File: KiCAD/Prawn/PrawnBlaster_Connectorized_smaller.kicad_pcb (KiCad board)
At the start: 2 copper layers, 93 x 58.4 mm, 37 parts, among them IC1 74LVT245D,118, J1 PWR SEL, J2 Ext. Clock, J3 Ext. Trig., J4 Pseudoclock 3, J5 Pseudoclock 1, J6 Pseudoclock 2, J7 Pseudoclock 0, J8 EXT PWR, U2 74LVC1G34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

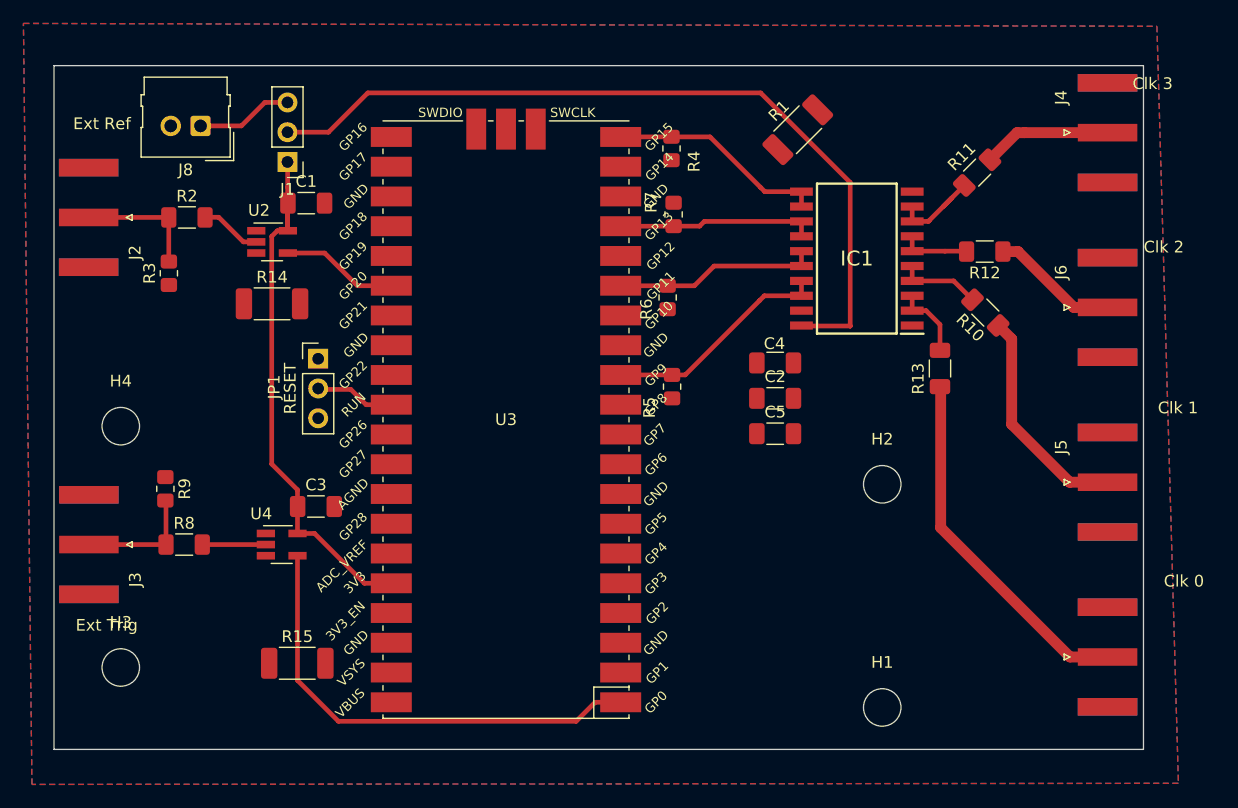
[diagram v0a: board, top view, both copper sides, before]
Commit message: Fixed trace and added gerber file
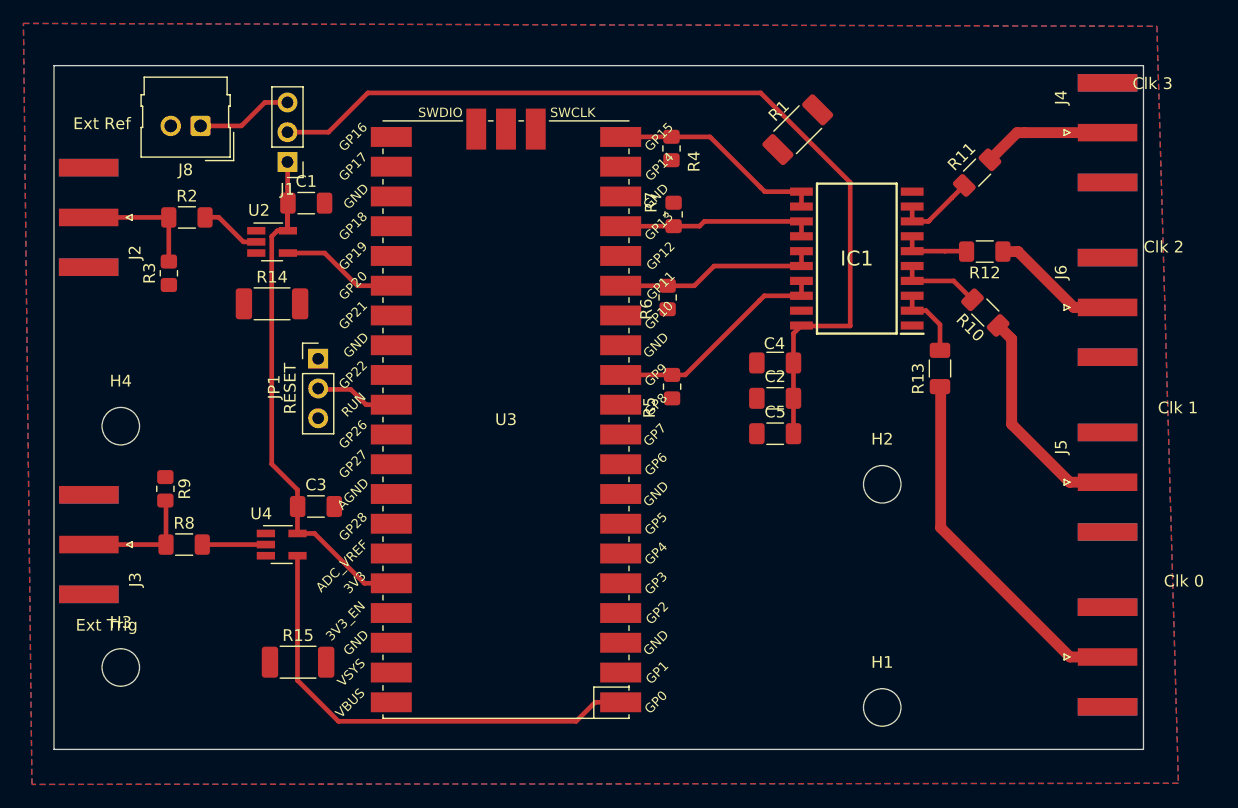
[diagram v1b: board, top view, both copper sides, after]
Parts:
- moved R15 0.11 mm to (107.9, 108.1)
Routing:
- net Power Supply: track 69.0 -> 78.5 mm
- net Net-(IC1-A6): track 8.03 -> 7.00 mm
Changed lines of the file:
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@@
   )
   (footprint "Resistor_SMD:R_2010_5025Metric_Pad1.40x2.65mm_HandSolder" (layer "F.Cu")
-    (at 107.8082 108.1804)
+    (at 107.876 108.0892)
     (descr "Resistor SMD 2010 (5025 Metric), square (rectangular) end terminal, IPC_7351 nominal with elongated pad for handsoldering. (Body size source: IPC-SM-782 page 72, https://www.pcb-3d.com/wordpress/wp-content/uploads/ipc-sm-782a_amendment_1_and_2.pdf), generated with kicad-footprint-generator")
     (tags "resistor handsolder")
@@
   (segment (start 134.5192 63.2462) (end 139.742 63.2462) (width 0.4) (layer "F.Cu") (net 6))
   (segment (start 139.752 63.2362) (end 139.762 63.2462) (width 0.4) (layer "F.Cu") (net 6))
-  (segment (start 162.947 69.1912) (end 163.677 68.4612) (width 0.4) (layer "F.Cu") (net 7))
   (segment (start 160.297 70.4612) (end 161.687 70.4612) (width 0.4) (layer "F.Cu") (net 7))
   (segment (start 161.742 70.3962) (end 163.677 68.4612) (width 0.4) (layer "F.Cu") (net 7))
@@
   (segment (start 113.6866 86.1108) (end 112.3796 84.8038) (width 0.4) (layer "F.Cu") (net 49))
   (segment (start 112.3796 84.8038) (end 109.6716 84.8038) (width 0.4) (layer "F.Cu") (net 49))
+  (segment (start 150.1642 80.034) (end 150.1642 88.5834) (width 0.4) (layer "F.Cu") (net 51))
   (segment (start 113.8262 59.4924) (end 147.3622 59.4924) (width 0.4) (layer "F.Cu") (net 51))
   (segment (start 110.4732 62.8454) (end 113.8262 59.4924) (width 0.4) (layer "F.Cu") (net 51))
@@
   (segment (start 106.9702 62.8454) (end 110.4732 62.8454) (width 0.4) (layer "F.Cu") (net 51))
   (segment (start 147.3622 59.4924) (end 155.0072 67.1374) (width 0.4) (layer "F.Cu") (net 51))
-  (segment (start 155.0046 79.3888) (end 155.012 79.3962) (width 0.4) (layer "F.Cu") (net 51))
-  (segment (start 155.0072 79.3862) (end 155.0046 79.3888) (width 0.4) (layer "F.Cu") (net 51))
   (segment (start 150.847 79.3512) (end 150.8846 79.3888) (width 0.4) (layer "F.Cu") (net 51))
+  (segment (start 150.847 79.3512) (end 150.1642 80.034) (width 0.4) (layer "F.Cu") (net 51))
   (segment (start 150.8846 79.3888) (end 155.0046 79.3888) (width 0.4) (layer "F.Cu") (net 51))
   (segment (start 103.0362 62.3094) (end 105.0402 60.3054) (width 0.4) (layer "F.Cu") (net 52))
